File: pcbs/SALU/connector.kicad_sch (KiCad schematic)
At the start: 13 parts, among them J201 Conn_02x20_Odd_Even, U201 74HC245, U202 74HC245

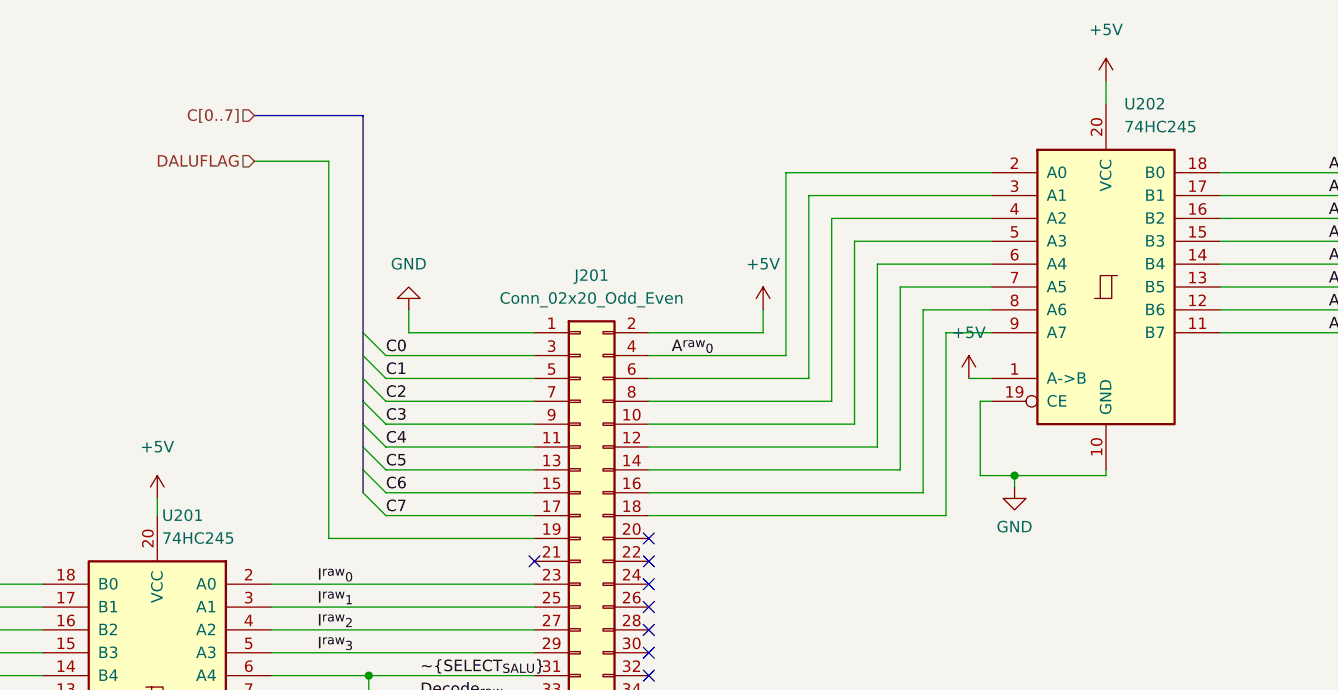
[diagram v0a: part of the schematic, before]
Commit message: Starting on inc/dec
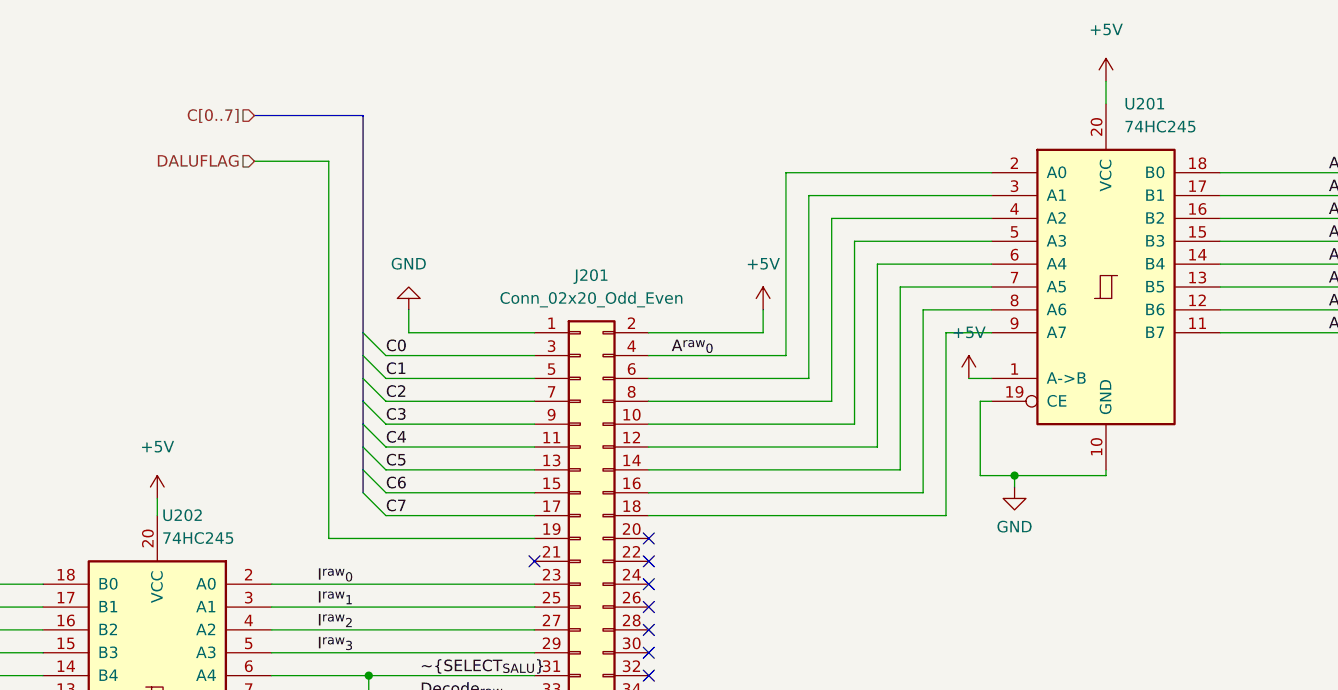
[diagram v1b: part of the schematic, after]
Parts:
- renumbered U202 to U201, U201 to U202
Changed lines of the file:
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@@
+    (stroke (width 0) (type default) (color 0 0 0 0))
+  )
+  (wire (pts (xy 60.325 70.485) (xy 60.325 72.39))
     (stroke (width 0) (type default) (color 0 0 0 0))
   )
@@
   )
   (wire (pts (xy 53.975 154.94) (xy 96.52 154.94))
-    (stroke (width 0) (type default) (color 0 0 0 0))
-  )
-  (wire (pts (xy 60.325 70.485) (xy 60.325 72.39))
     (stroke (width 0) (type default) (color 0 0 0 0))
   )
@@
   (symbol (lib_id "power:GND") (at 60.325 113.665 0) (unit 1)
     (in_bom yes) (on_board yes) (fields_autoplaced)
-    (property "Reference" "#PWR0106" (id 0) (at 60.325 120.015 0)
+    (property "Reference" "#PWR0210" (id 0) (at 60.325 120.015 0)
       (effects (font (size 1.27 1.27)) hide)
     )
@@
   (symbol (lib_id "power:+5V") (at 60.325 70.485 0) (unit 1)
     (in_bom yes) (on_board yes) (fields_autoplaced)
-    (property "Reference" "#PWR0102" (id 0) (at 60.325 74.295 0)
+    (property "Reference" "#PWR0206" (id 0) (at 60.325 74.295 0)
       (effects (font (size 1.27 1.27)) hide)
     )
@@
   (symbol (lib_id "power:GND") (at 88.265 102.87 0) (unit 1)
     (in_bom yes) (on_board yes) (fields_autoplaced)
-    (property "Reference" "#PWR0107" (id 0) (at 88.265 109.22 0)
+    (property "Reference" "#PWR0208" (id 0) (at 88.265 109.22 0)
       (effects (font (size 1.27 1.27)) hide)
     )
@@
   (symbol (lib_id "power:PWR_FLAG") (at 97.155 100.33 180) (unit 1)
     (in_bom yes) (on_board yes) (fields_autoplaced)
-    (property "Reference" "#FLG0101" (id 0) (at 97.155 102.235 0)
+    (property "Reference" "#FLG0201" (id 0) (at 97.155 102.235 0)
       (effects (font (size 1.27 1.27)) hide)
     )
@@
   (symbol (lib_id "power:+5V") (at 127.635 102.87 180) (unit 1)
     (in_bom yes) (on_board yes) (fields_autoplaced)
-    (property "Reference" "#PWR0109" (id 0) (at 127.635 99.06 0)
+    (property "Reference" "#PWR0209" (id 0) (at 127.635 99.06 0)
       (effects (font (size 1.27 1.27)) hide)
     )
@@
   (symbol (lib_id "power:+5V") (at 109.22 154.94 270) (unit 1)
     (in_bom yes) (on_board yes) (fields_autoplaced)
-    (property "Reference" "#PWR0105" (id 0) (at 105.41 154.94 0)
+    (property "Reference" "#PWR0214" (id 0) (at 105.41 154.94 0)
       (effects (font (size 1.27 1.27)) hide)
     )
@@
   (symbol (lib_id "power:GND") (at 88.265 49.53 180) (unit 1)
     (in_bom yes) (on_board yes) (fields_autoplaced)
-    (property "Reference" "#PWR0101" (id 0) (at 88.265 43.18 0)
+    (property "Reference" "#PWR0202" (id 0) (at 88.265 43.18 0)
       (effects (font (size 1.27 1.27)) hide)
     )
@@
   (symbol (lib_id "power:+5V") (at 196.85 130.81 0) (unit 1)
     (in_bom yes) (on_board yes) (fields_autoplaced)
-    (property "Reference" "#PWR0114" (id 0) (at 196.85 134.62 0)
+    (property "Reference" "#PWR0212" (id 0) (at 196.85 134.62 0)
       (effects (font (size 1.27 1.27)) hide)
     )
@@
   (symbol (lib_id "power:GND") (at 110.49 179.07 90) (mirror x) (unit 1)
     (in_bom yes) (on_board yes) (fields_autoplaced)
-    (property "Reference" "#PWR0104" (id 0) (at 116.84 179.07 0)
+    (property "Reference" "#PWR0215" (id 0) (at 116.84 179.07 0)
       (effects (font (size 1.27 1.27)) hide)
     )
@@
   (symbol (lib_id "power:GND") (at 155.575 69.215 0) (unit 1)
     (in_bom yes) (on_board yes) (fields_autoplaced)
-    (property "Reference" "#PWR0110" (id 0) (at 155.575 75.565 0)
+    (property "Reference" "#PWR0205" (id 0) (at 155.575 75.565 0)
       (effects (font (size 1.27 1.27)) hide)
     )
@@
   (symbol (lib_id "power:GND") (at 197.485 142.875 0) (unit 1)
     (in_bom yes) (on_board yes) (fields_autoplaced)
-    (property "Reference" "#PWR0115" (id 0) (at 197.485 149.225 0)
+    (property "Reference" "#PWR0213" (id 0) (at 197.485 149.225 0)
       (effects (font (size 1.27 1.27)) hide)
     )
@@
   (symbol (lib_id "74xx:74HC245") (at 60.325 92.71 0) (mirror y) (unit 1)
     (in_bom yes) (on_board yes) (fields_autoplaced)
-    (property "Reference" "U201" (id 0) (at 60.8456 72.39 0)
+    (property "Reference" "U202" (id 0) (at 60.8456 72.39 0)
       (effects (font (size 1.27 1.27)) (justify right))
     )
@@
   (symbol (lib_id "74xx:74HC245") (at 165.735 46.99 0) (unit 1)
     (in_bom yes) (on_board yes) (fields_autoplaced)
-    (property "Reference" "U202" (id 0) (at 167.7544 26.67 0)
+    (property "Reference" "U201" (id 0) (at 167.7544 26.67 0)
       (effects (font (size 1.27 1.27)) (justify left))
     )
@@
   (symbol (lib_id "power:PWR_FLAG") (at 118.745 100.33 180) (unit 1)
     (in_bom yes) (on_board yes) (fields_autoplaced)
-    (property "Reference" "#FLG0102" (id 0) (at 118.745 102.235 0)
+    (property "Reference" "#FLG0202" (id 0) (at 118.745 102.235 0)
       (effects (font (size 1.27 1.27)) hide)
     )
@@
   (symbol (lib_id "power:+5V") (at 150.495 57.15 0) (unit 1)
     (in_bom yes) (on_board yes) (fields_autoplaced)
-    (property "Reference" "#PWR0112" (id 0) (at 150.495 60.96 0)
+    (property "Reference" "#PWR0204" (id 0) (at 150.495 60.96 0)
       (effects (font (size 1.27 1.27)) hide)
     )
@@
   (symbol (lib_id "power:+5V") (at 76.2 102.87 270) (unit 1)
     (in_bom yes) (on_board yes) (fields_autoplaced)
-    (property "Reference" "#PWR0108" (id 0) (at 72.39 102.87 0)
+    (property "Reference" "#PWR0207" (id 0) (at 72.39 102.87 0)
       (effects (font (size 1.27 1.27)) hide)
     )
@@
   (symbol (lib_id "power:+5V") (at 127.635 49.53 0) (unit 1)
     (in_bom yes) (on_board yes) (fields_autoplaced)
-    (property "Reference" "#PWR0111" (id 0) (at 127.635 53.34 0)
+    (property "Reference" "#PWR0203" (id 0) (at 127.635 53.34 0)
       (effects (font (size 1.27 1.27)) hide)
     )
@@
   (symbol (lib_id "power:GND") (at 110.49 130.175 90) (mirror x) (unit 1)
     (in_bom yes) (on_board yes) (fields_autoplaced)
-    (property "Reference" "#PWR0103" (id 0) (at 116.84 130.175 0)
+    (property "Reference" "#PWR0211" (id 0) (at 116.84 130.175 0)
       (effects (font (size 1.27 1.27)) hide)
     )
@@
   (symbol (lib_id "power:+5V") (at 165.735 24.13 0) (unit 1)
     (in_bom yes) (on_board yes) (fields_autoplaced)
-    (property "Reference" "#PWR0113" (id 0) (at 165.735 27.94 0)
-      (effects (font (size 1.27 1.27)) hide)
-    )
+    (property "Reference" "#PWR0201" (id 0) (at 165.735 27.94 0)
+      (effects (font (size 1.27 1.27)) hide)
+    )

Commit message: Some more functions
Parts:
- renumbered U202 to U201, U201 to U202
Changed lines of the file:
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@@
   (symbol (lib_id "power:GND") (at 60.325 113.665 0) (unit 1)
     (in_bom yes) (on_board yes) (fields_autoplaced)
-    (property "Reference" "#PWR0210" (id 0) (at 60.325 120.015 0)
+    (property "Reference" "#PWR0202" (id 0) (at 60.325 120.015 0)
       (effects (font (size 1.27 1.27)) hide)
     )
@@
   (symbol (lib_id "power:+5V") (at 60.325 70.485 0) (unit 1)
     (in_bom yes) (on_board yes) (fields_autoplaced)
-    (property "Reference" "#PWR0206" (id 0) (at 60.325 74.295 0)
+    (property "Reference" "#PWR0201" (id 0) (at 60.325 74.295 0)
       (effects (font (size 1.27 1.27)) hide)
     )
@@
   (symbol (lib_id "power:GND") (at 88.265 102.87 0) (unit 1)
     (in_bom yes) (on_board yes) (fields_autoplaced)
-    (property "Reference" "#PWR0208" (id 0) (at 88.265 109.22 0)
+    (property "Reference" "#PWR0205" (id 0) (at 88.265 109.22 0)
       (effects (font (size 1.27 1.27)) hide)
     )
@@
   (symbol (lib_id "power:+5V") (at 127.635 102.87 180) (unit 1)
     (in_bom yes) (on_board yes) (fields_autoplaced)
-    (property "Reference" "#PWR0209" (id 0) (at 127.635 99.06 0)
+    (property "Reference" "#PWR0210" (id 0) (at 127.635 99.06 0)
       (effects (font (size 1.27 1.27)) hide)
     )
@@
   (symbol (lib_id "power:+5V") (at 109.22 154.94 270) (unit 1)
     (in_bom yes) (on_board yes) (fields_autoplaced)
-    (property "Reference" "#PWR0214" (id 0) (at 105.41 154.94 0)
+    (property "Reference" "#PWR0206" (id 0) (at 105.41 154.94 0)
       (effects (font (size 1.27 1.27)) hide)
     )
@@
   (symbol (lib_id "power:GND") (at 88.265 49.53 180) (unit 1)
     (in_bom yes) (on_board yes) (fields_autoplaced)
-    (property "Reference" "#PWR0202" (id 0) (at 88.265 43.18 0)
+    (property "Reference" "#PWR0204" (id 0) (at 88.265 43.18 0)
       (effects (font (size 1.27 1.27)) hide)
     )
@@
   (symbol (lib_id "power:+5V") (at 196.85 130.81 0) (unit 1)
     (in_bom yes) (on_board yes) (fields_autoplaced)
-    (property "Reference" "#PWR0212" (id 0) (at 196.85 134.62 0)
+    (property "Reference" "#PWR0214" (id 0) (at 196.85 134.62 0)
       (effects (font (size 1.27 1.27)) hide)
     )
@@
   (symbol (lib_id "power:GND") (at 110.49 179.07 90) (mirror x) (unit 1)
     (in_bom yes) (on_board yes) (fields_autoplaced)
-    (property "Reference" "#PWR0215" (id 0) (at 116.84 179.07 0)
+    (property "Reference" "#PWR0208" (id 0) (at 116.84 179.07 0)
       (effects (font (size 1.27 1.27)) hide)
     )
@@
   (symbol (lib_id "power:GND") (at 155.575 69.215 0) (unit 1)
     (in_bom yes) (on_board yes) (fields_autoplaced)
-    (property "Reference" "#PWR0205" (id 0) (at 155.575 75.565 0)
+    (property "Reference" "#PWR0212" (id 0) (at 155.575 75.565 0)
       (effects (font (size 1.27 1.27)) hide)
     )
@@
   (symbol (lib_id "power:GND") (at 197.485 142.875 0) (unit 1)
     (in_bom yes) (on_board yes) (fields_autoplaced)
-    (property "Reference" "#PWR0213" (id 0) (at 197.485 149.225 0)
+    (property "Reference" "#PWR0215" (id 0) (at 197.485 149.225 0)
       (effects (font (size 1.27 1.27)) hide)
     )
@@
   (symbol (lib_id "74xx:74HC245") (at 60.325 92.71 0) (mirror y) (unit 1)
     (in_bom yes) (on_board yes) (fields_autoplaced)
-    (property "Reference" "U202" (id 0) (at 60.8456 72.39 0)
+    (property "Reference" "U201" (id 0) (at 60.8456 72.39 0)
       (effects (font (size 1.27 1.27)) (justify right))
     )
@@
   (symbol (lib_id "74xx:74HC245") (at 165.735 46.99 0) (unit 1)
     (in_bom yes) (on_board yes) (fields_autoplaced)
-    (property "Reference" "U201" (id 0) (at 167.7544 26.67 0)
+    (property "Reference" "U202" (id 0) (at 167.7544 26.67 0)
       (effects (font (size 1.27 1.27)) (justify left))
     )
@@
   (symbol (lib_id "power:+5V") (at 150.495 57.15 0) (unit 1)
     (in_bom yes) (on_board yes) (fields_autoplaced)
-    (property "Reference" "#PWR0204" (id 0) (at 150.495 60.96 0)
+    (property "Reference" "#PWR0211" (id 0) (at 150.495 60.96 0)
       (effects (font (size 1.27 1.27)) hide)
     )
@@
   (symbol (lib_id "power:+5V") (at 76.2 102.87 270) (unit 1)
     (in_bom yes) (on_board yes) (fields_autoplaced)
-    (property "Reference" "#PWR0207" (id 0) (at 72.39 102.87 0)
+    (property "Reference" "#PWR0203" (id 0) (at 72.39 102.87 0)
       (effects (font (size 1.27 1.27)) hide)
     )
@@
   (symbol (lib_id "power:+5V") (at 127.635 49.53 0) (unit 1)
     (in_bom yes) (on_board yes) (fields_autoplaced)
-    (property "Reference" "#PWR0203" (id 0) (at 127.635 53.34 0)
+    (property "Reference" "#PWR0209" (id 0) (at 127.635 53.34 0)
       (effects (font (size 1.27 1.27)) hide)
     )
@@
   (symbol (lib_id "power:GND") (at 110.49 130.175 90) (mirror x) (unit 1)
     (in_bom yes) (on_board yes) (fields_autoplaced)
-    (property "Reference" "#PWR0211" (id 0) (at 116.84 130.175 0)
+    (property "Reference" "#PWR0207" (id 0) (at 116.84 130.175 0)
       (effects (font (size 1.27 1.27)) hide)
     )
@@
   (symbol (lib_id "power:+5V") (at 165.735 24.13 0) (unit 1)
     (in_bom yes) (on_board yes) (fields_autoplaced)
-    (property "Reference" "#PWR0201" (id 0) (at 165.735 27.94 0)
-      (effects (font (size 1.27 1.27)) hide)
-    )
+    (property "Reference" "#PWR0213" (id 0) (at 165.735 27.94 0)
+      (effects (font (size 1.27 1.27)) hide)
+    )

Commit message: Routing
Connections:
- net DALUFLAG renamed SALUFLAG
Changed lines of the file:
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@@
     (effects (font (size 1.27 1.27)) (justify left))
   )
-  (hierarchical_label "DALUFLAG" (shape input) (at 71.12 33.02 180)
+  (hierarchical_label "SALUFLAG" (shape input) (at 71.12 33.02 180)
     (effects (font (size 1.27 1.27)) (justify right))
   )
